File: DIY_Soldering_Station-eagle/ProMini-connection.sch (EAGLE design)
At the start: 45 parts, among them IC1 LM358N, Q1 IRLZ44Z, Q2 IRLZ44Z, T1 BT136, X1 6ESRM-P, X2 HD44780LCD-1602

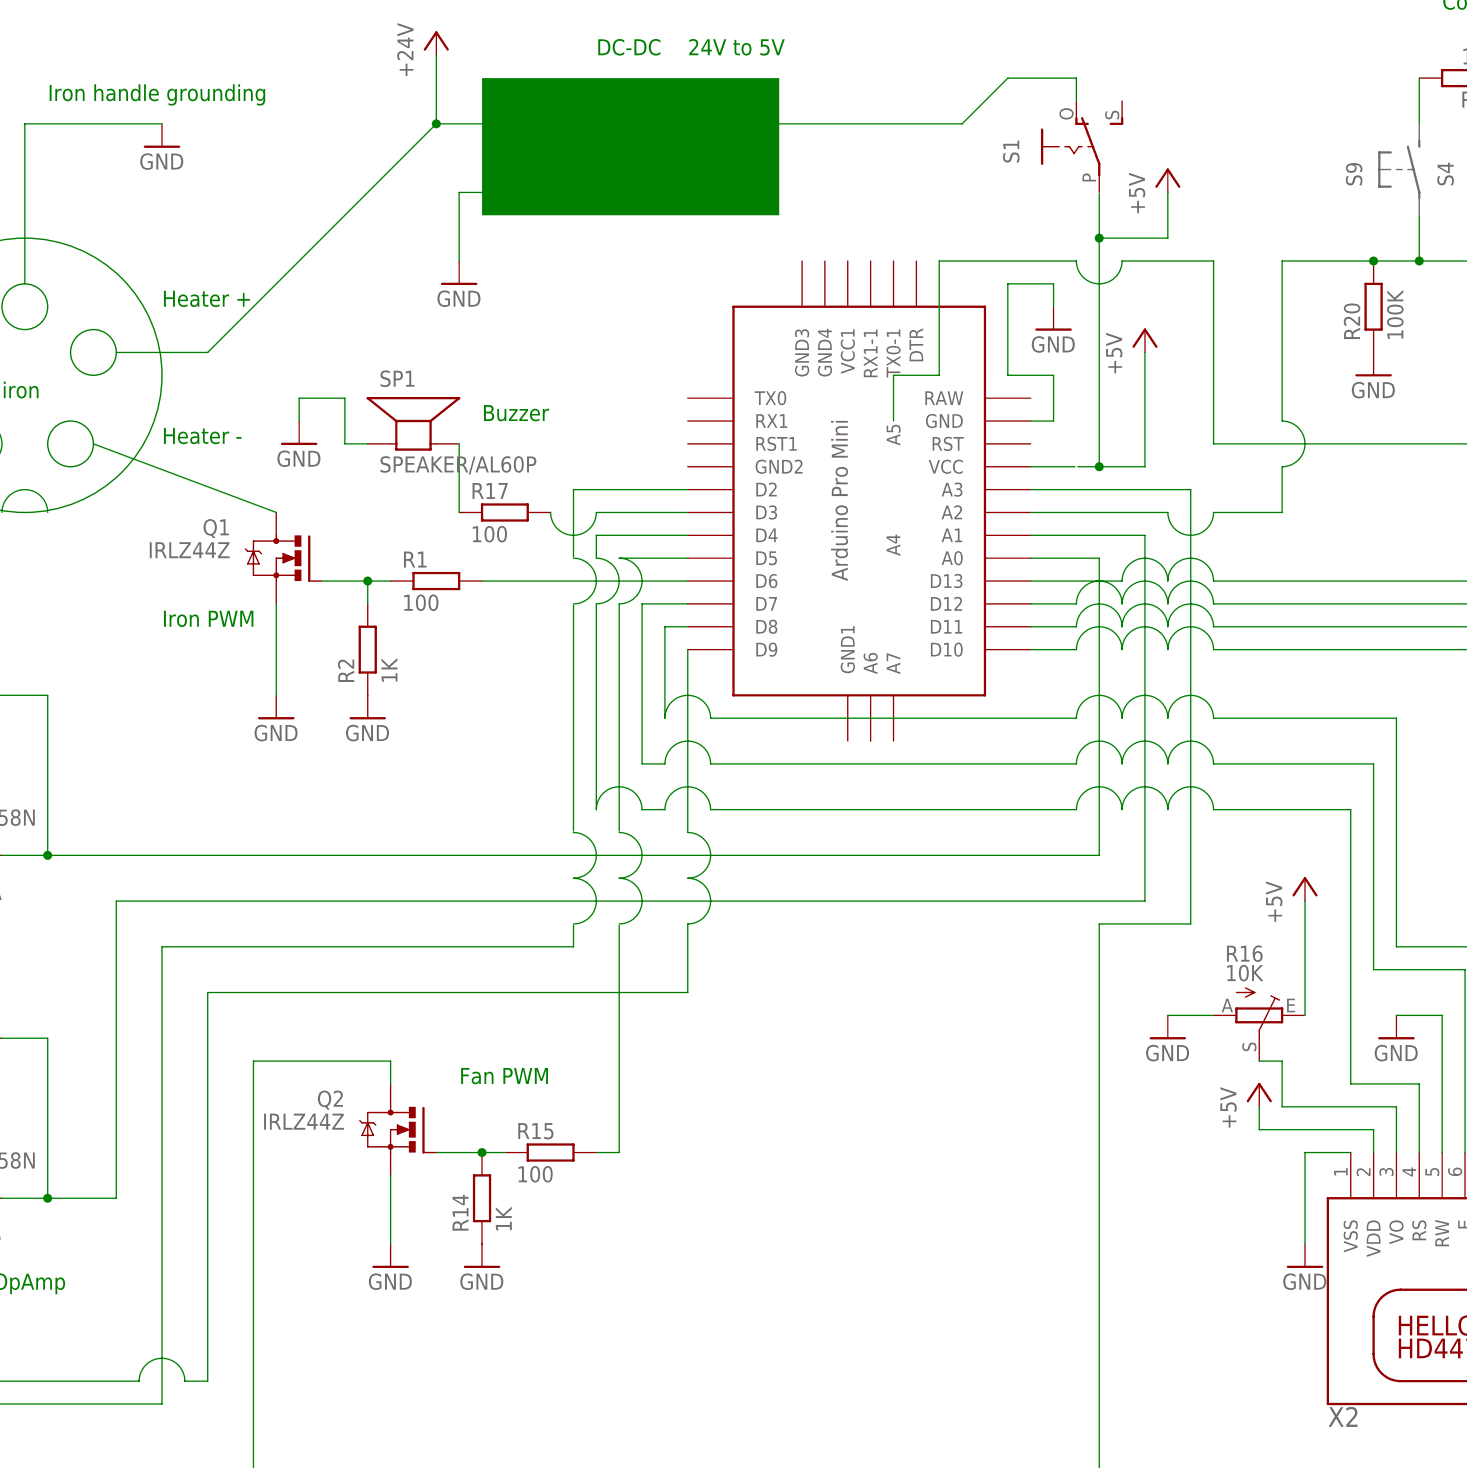
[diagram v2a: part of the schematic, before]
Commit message: replace some pins to save A3 pin
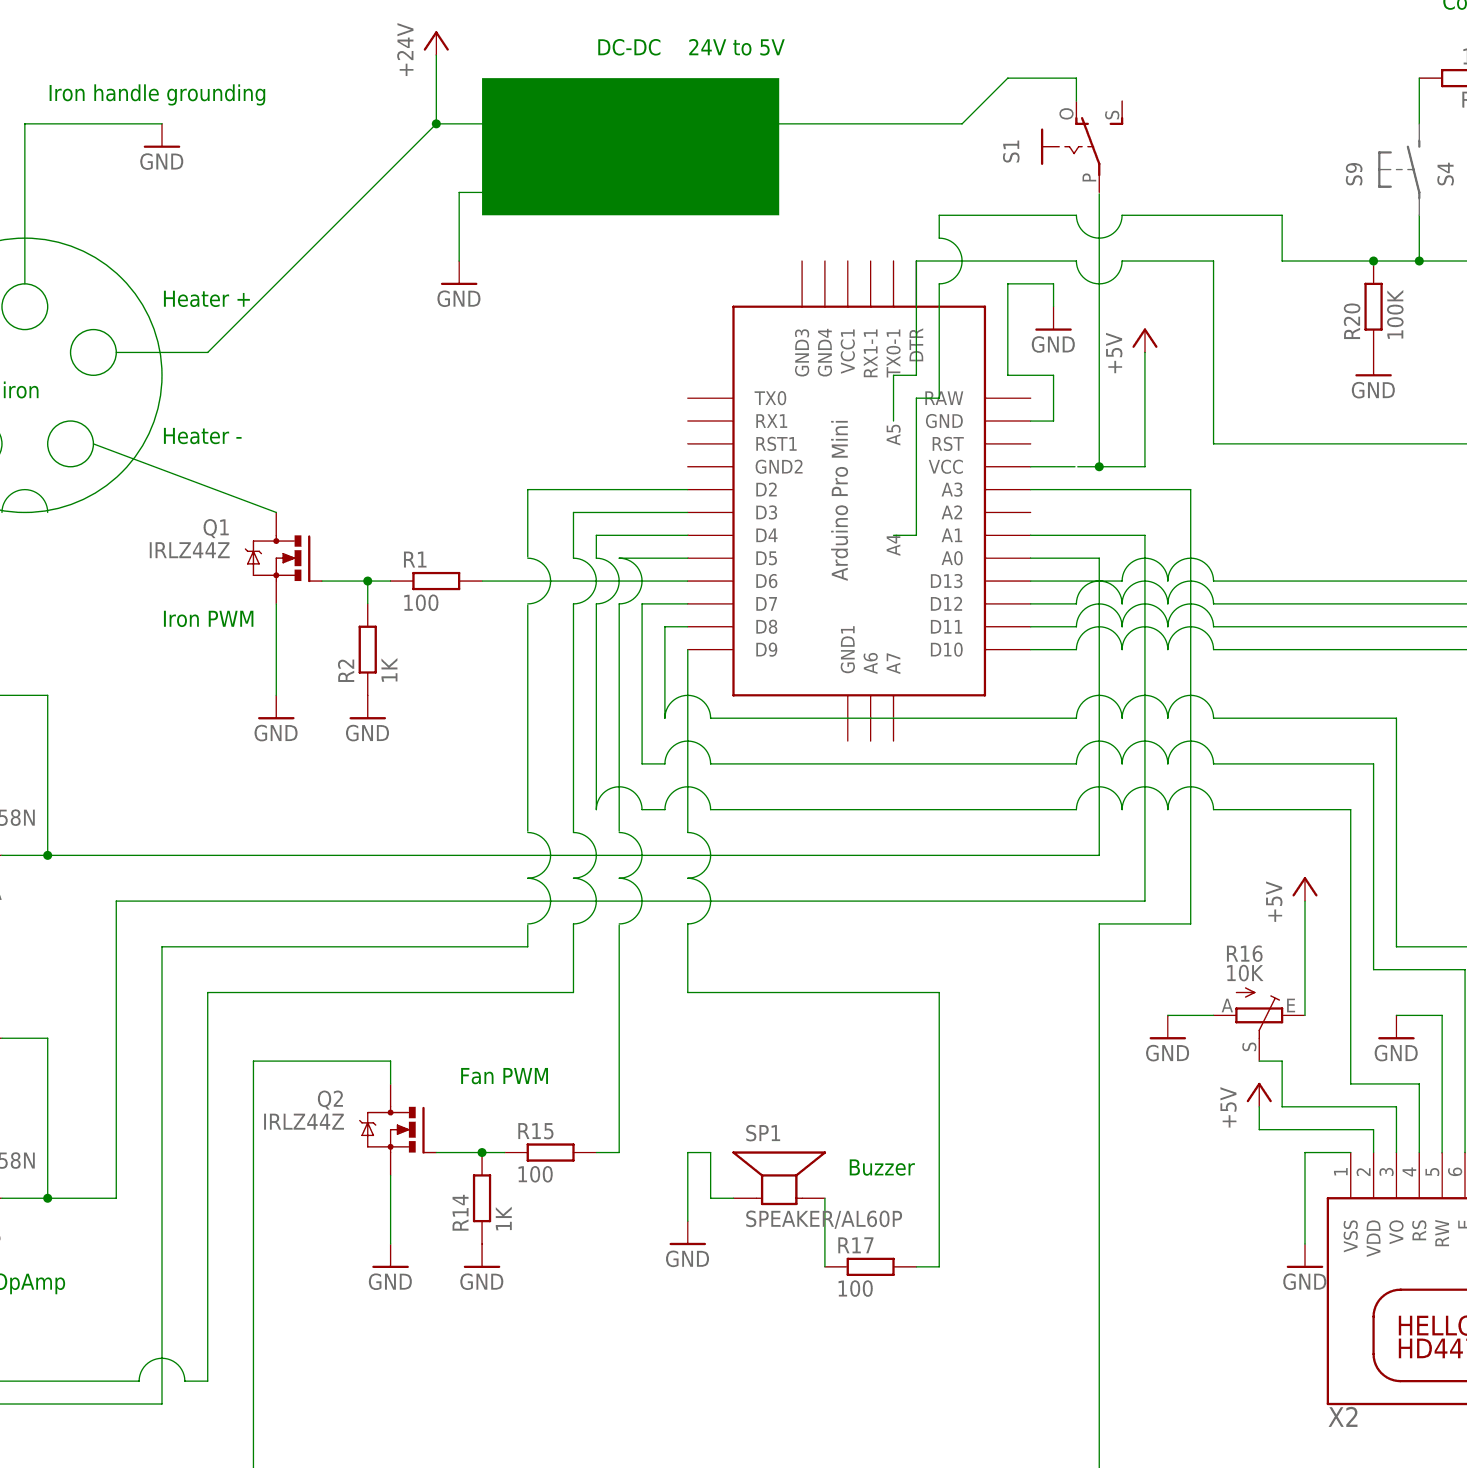
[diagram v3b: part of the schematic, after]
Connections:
- net N$22: now also R17.2; no longer R13.1
- net N$40: now also R13.1; no longer R17.2
- net N$50: no longer U$1.A2
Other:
- moved on the sheet: R17, SP1
